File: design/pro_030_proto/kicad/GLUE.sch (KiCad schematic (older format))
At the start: 26 parts, among them IC3 ATF16V8BQL-15PU

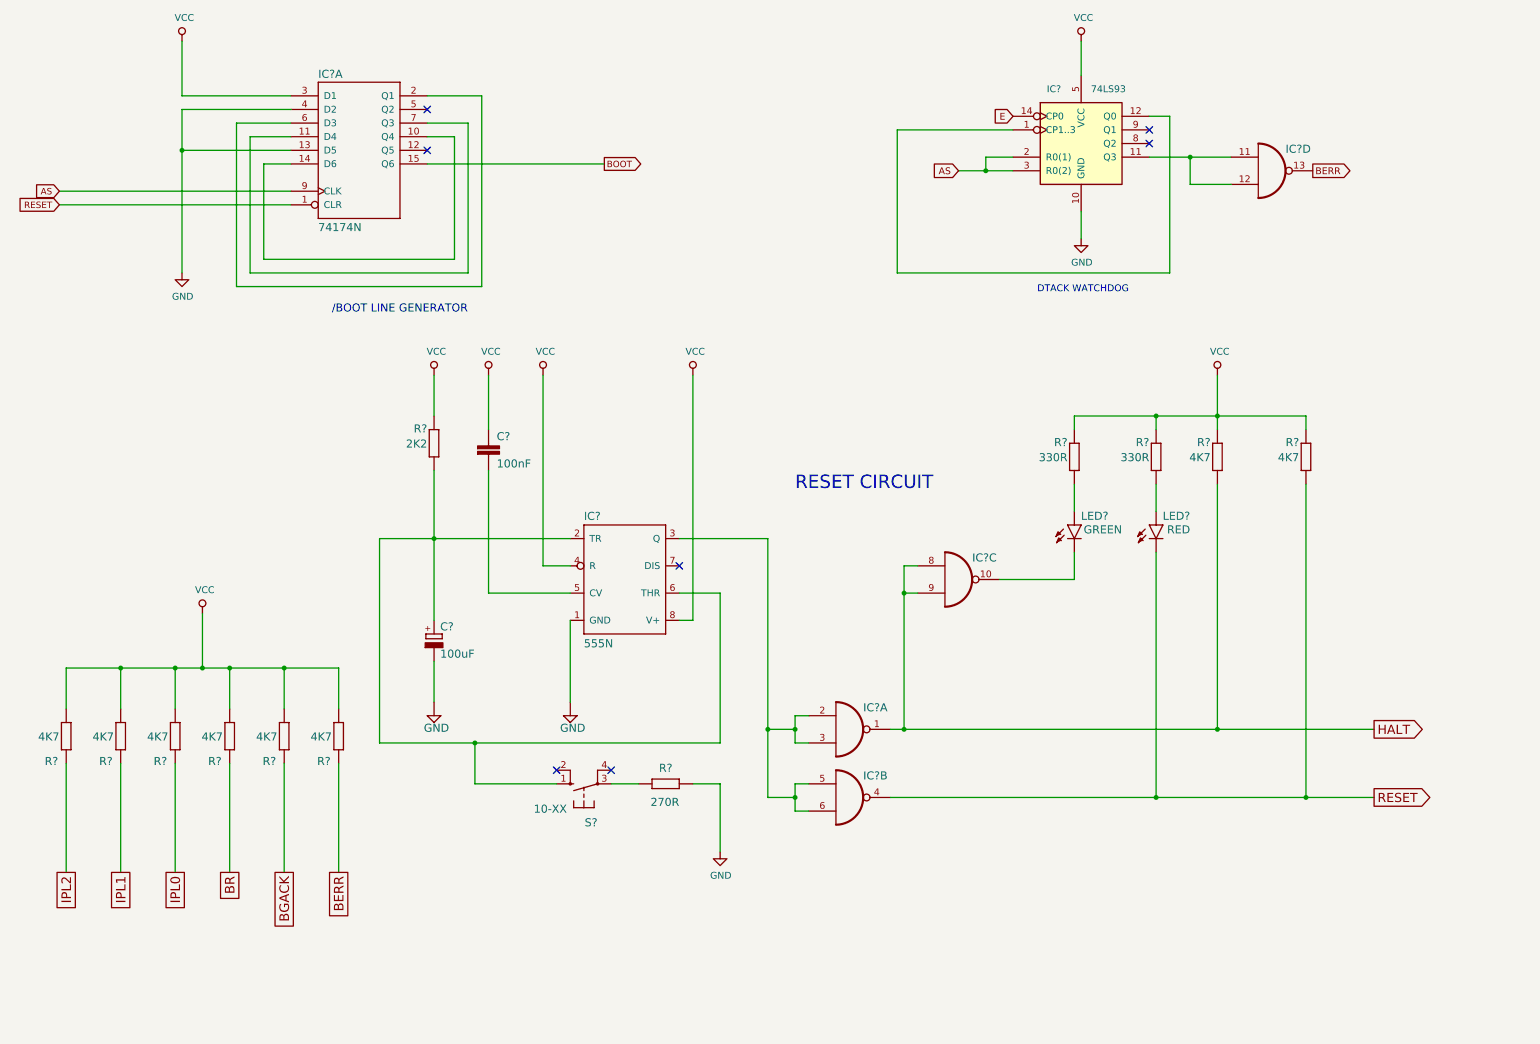
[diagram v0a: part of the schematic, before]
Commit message: Add interrupt glue to schematic
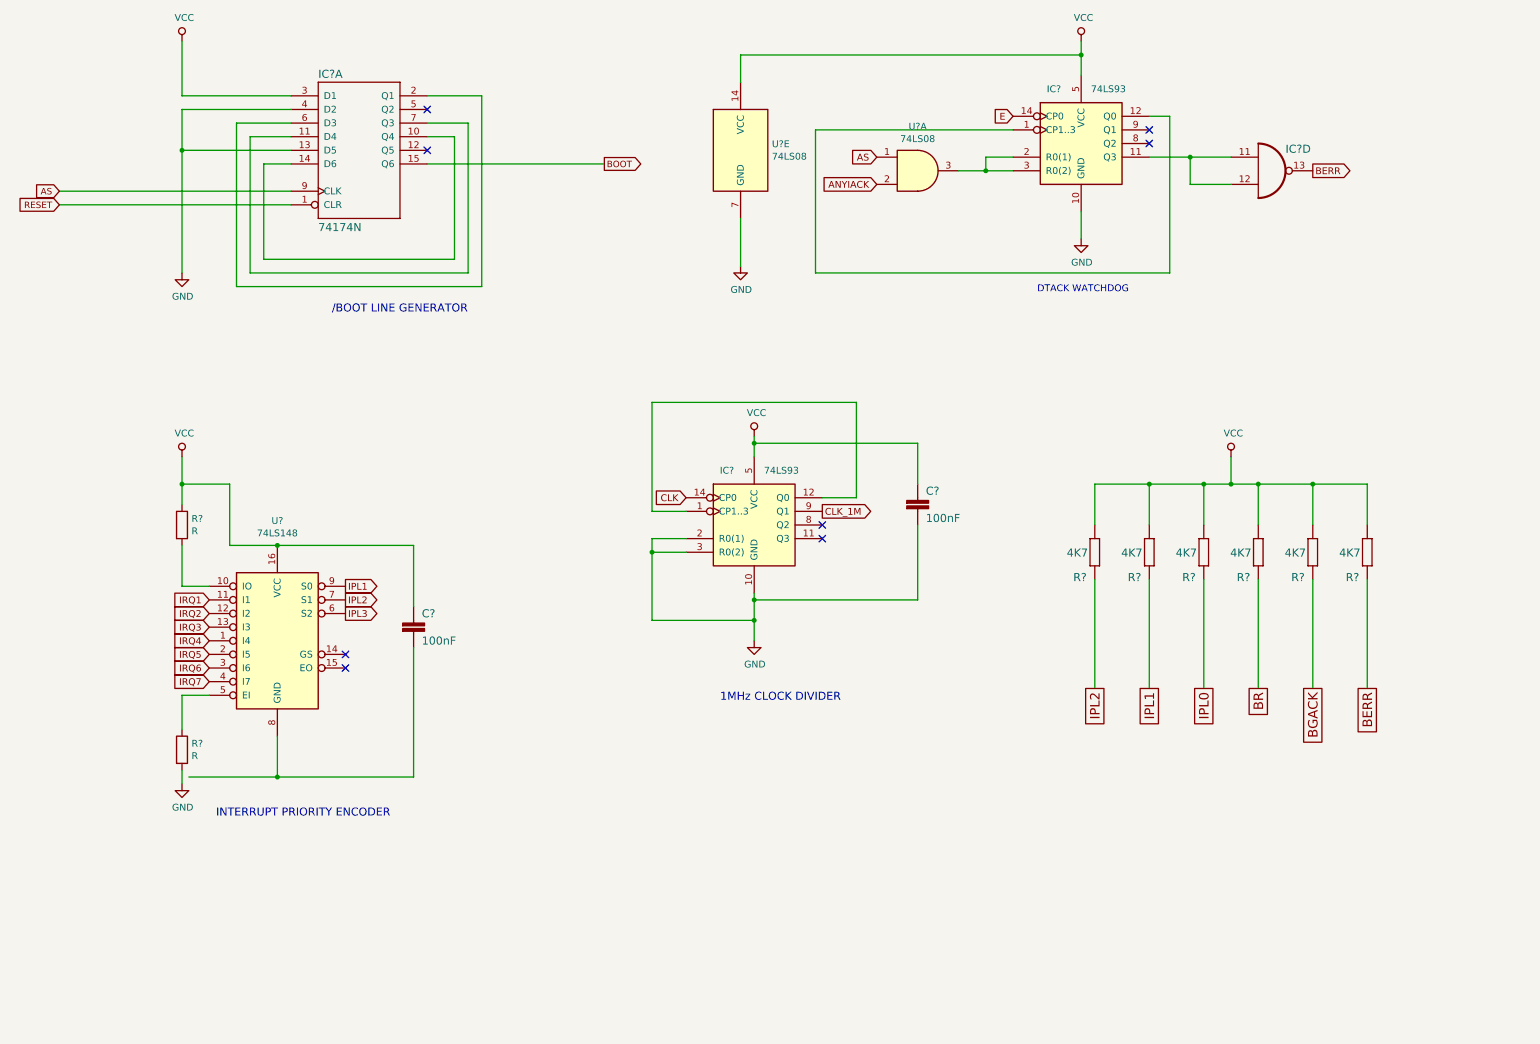
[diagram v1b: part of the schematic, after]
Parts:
- removed C?: 100nF, rosco_m68k:C2.5-3, symbol rosco_m68k-eagle-import:C2,5-3
- removed C?: 100uF, rosco_m68k:E2,5-5, symbol rosco_m68k-eagle-import:CPOL-EUE2.5-5
- removed IC?: 555N, Package_DIP:DIP-8_W7.62mm_LongPads, symbol rosco_m68k-eagle-import:555N
- removed IC? (x3): 74LS01N, Package_DIP:DIP-14_W7.62mm_Socket_LongPads, symbol rosco_m68k-eagle-import:7401N
- removed LED?: RED, rosco_m68k:LED5MM, symbol rosco_m68k-eagle-import:LED5MM
- removed LED?: GREEN, rosco_m68k:LED5MM, symbol rosco_m68k-eagle-import:LED5MM
- removed R?: 2K2, rosco_m68k:0207_10, symbol rosco_m68k-eagle-import:R-EU_0207_10
- removed R?: 270R, rosco_m68k:0207_10, symbol rosco_m68k-eagle-import:R-EU_0207_10
- removed R? (x2): 330R, rosco_m68k:0207_10, symbol rosco_m68k-eagle-import:R-EU_0207_10
- removed R? (x2): 4K7, rosco_m68k:0207_10, symbol rosco_m68k-eagle-import:R-EU_0207_10
- removed S?: 10-XX, rosco_m68k:B3F-10XX, symbol rosco_m68k-eagle-import:10-XX
- added C? (x2): 100nF, rosco_m68k:C2.5-3, symbol rosco_m68k-eagle-import:C2,5-3
- added IC?: 74LS93, Package_DIP:DIP-14_W7.62mm_Socket_LongPads, symbol 74xx:74LS93
- added R? (x2): R, symbol Device:R
- added U? (x2): 74LS08, symbol 74xx:74LS08
- added U?: 74LS148, symbol 74xx:74LS148
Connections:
- net labels added: ANYIACK, CLK, CLK_1M, IPL3, IRQ1, IRQ2, IRQ3, IRQ4, IRQ5, IRQ6, IRQ7
- net labels removed: HALT
- wire segments 139 -> 116
- no-connect marks 9 -> 10
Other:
- note added: "1MHz CLOCK DIVIDER"
- note added: "INTERRUPT PRIORITY ENCODER"
- note removed: "RESET CIRCUIT"
- moved on the sheet: R?

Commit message: Largeish changeset:
* Added (first-cut) glue for DTACK generation
* Fix mem selects to use new DTACK generation
* Add missing footprints for Kicad
* Add POWER and TESTPOINTS schematics
* Update footprints across the board to allow error-free PCB import
* Pull all components (so far) into PCB
* Fix MC68030RC footprint (missing pads)
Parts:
- removed C13: 100nF, rosco_m68k:C2.5-3, symbol rosco_m68k-eagle-import:C2,5-3
- removed IC3: ATF16V8BQL-15PU, rosco_m68k:DIL20, symbol rosco_m68k-eagle-import:ATF16V8BP3
- removed R? (x6): 4K7, rosco_m68k:0207_10, symbol rosco_m68k-eagle-import:R-EU_0207_10
- removed U?: 74LS08, symbol 74xx:74LS08
- added X2: 8MHz, Oscillator:Oscillator_DIP-8, symbol Oscillator:CXO_DIP8
- IC12: renamed from U?; footprint (none) -> Package_DIP:DIP-16_W7.62mm_Socket_LongPads
- IC13: renamed from U?; footprint (none) -> Package_DIP:DIP-14_W7.62mm_LongPads
- R24, R25: renamed from R?; footprint (none) -> rosco_m68k:R-0207_10
- gave numbers to parts that had none: 6
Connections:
- net labels added: CLK_8M
- net labels removed: A10, A11, A12, A13, A14, A15, A16, A17, A18, A6, A7, A8, A9, A[1..23], BGACK, BR, CLK, IOSEL, IPL0, LDS, MFPSEL
- wire segments 116 -> 83
- no-connect marks 10 -> 8
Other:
- note added: "8MHz/1MHz PERIPHERAL CLOCK"
- note removed: "1MHz CLOCK DIVIDER"
- note removed: "MFPSEL.PLD"
- moved on the sheet: C5

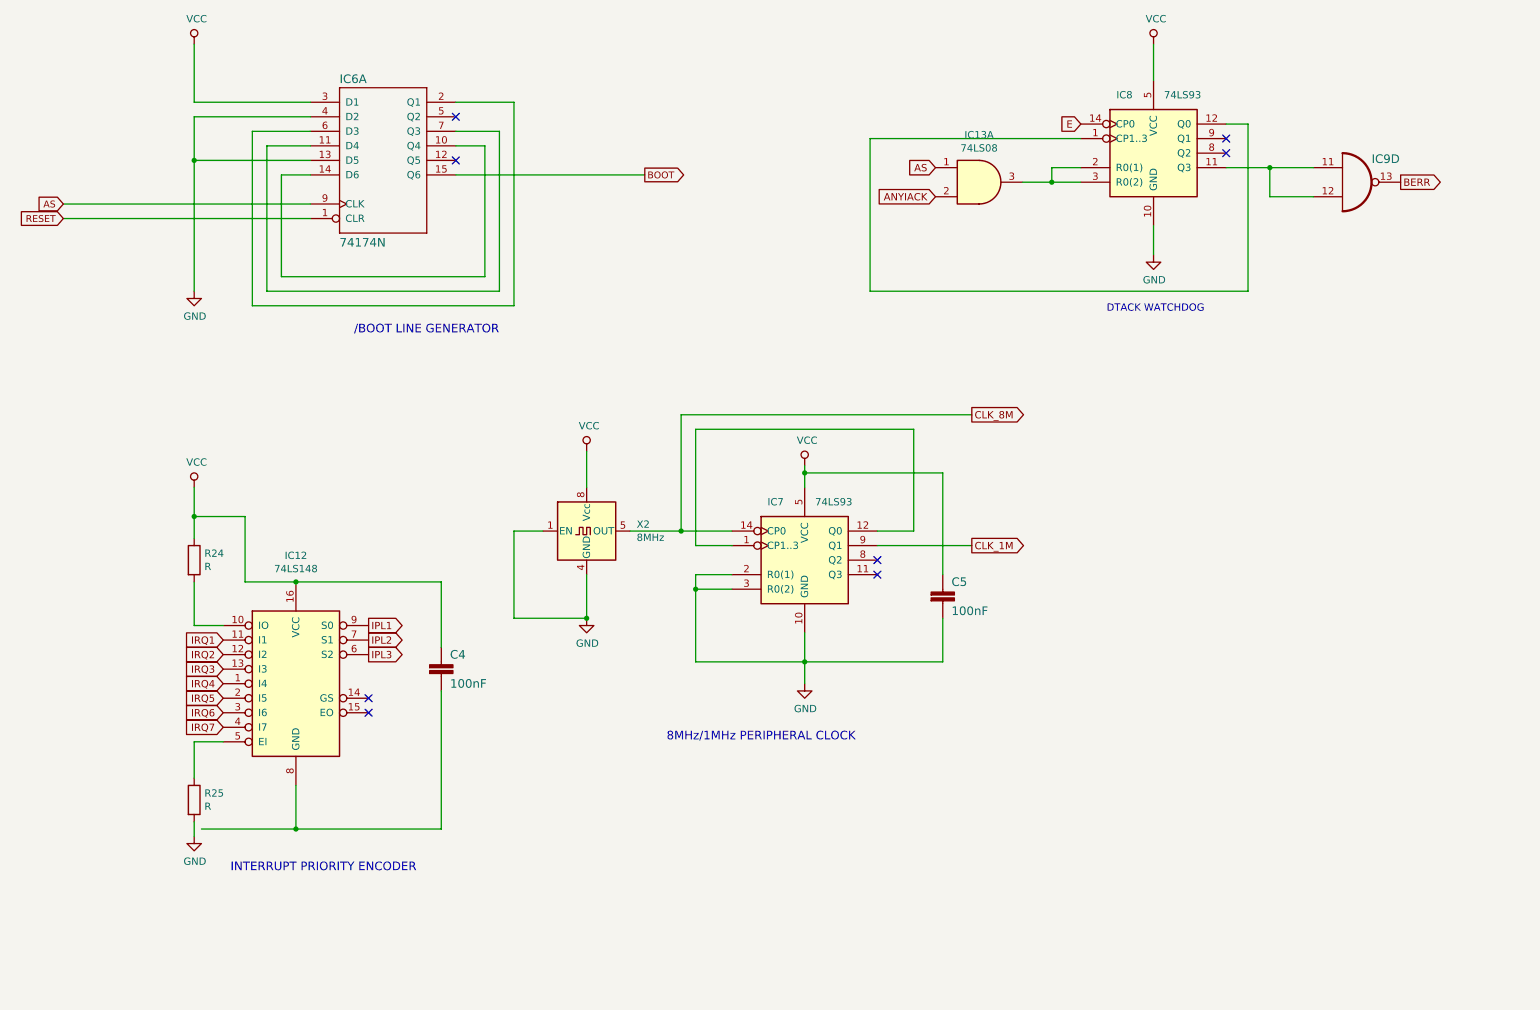
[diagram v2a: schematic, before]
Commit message: Add DTACK delays and fixes
* Add configurable DTACK delay for RAM & ROM
* Add DTACK generation for RAM/ROM with delay support in IC5
* Fix /BOOT line generator for 32-bit port
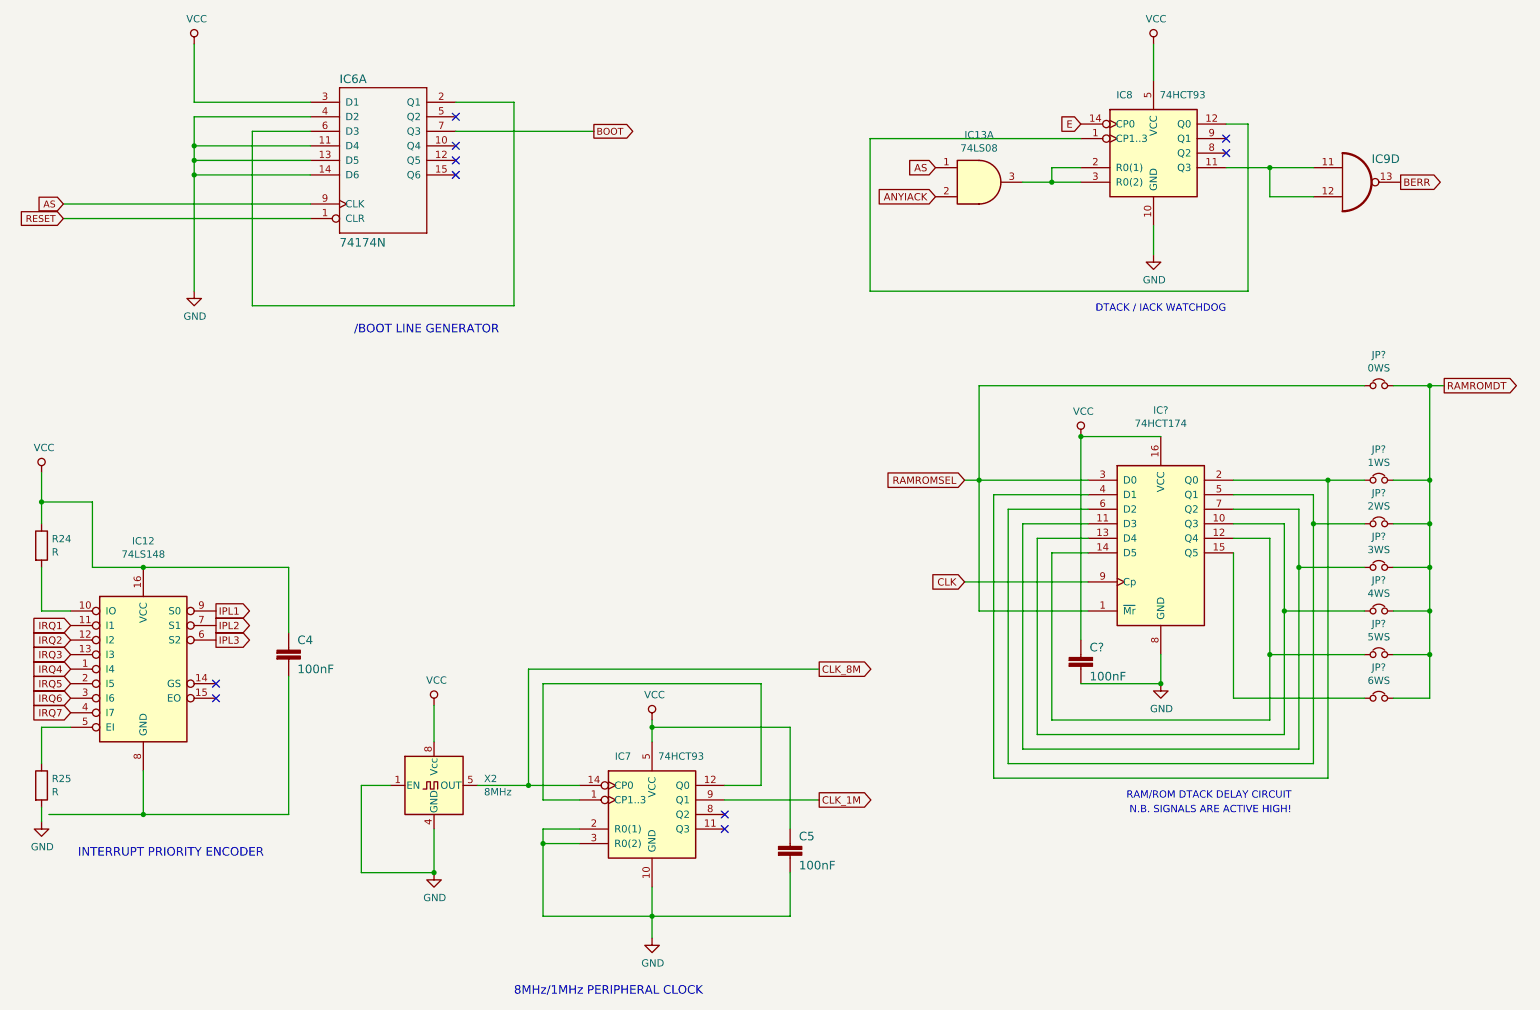
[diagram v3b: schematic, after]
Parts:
- added C?: 100nF, rosco_m68k:C2.5-3, symbol rosco_m68k-eagle-import:C2,5-3
- added IC?: 74HCT174, Package_DIP:DIP-16_W7.62mm_Socket_LongPads, symbol 74xx:74LS174
- added JP?: 0WS, rosco_m68k:pin-1X02, symbol Device:Jumper_NC_Small
- added JP?: 1WS, rosco_m68k:pin-1X02, symbol Device:Jumper_NC_Small
- added JP?: 2WS, rosco_m68k:pin-1X02, symbol Device:Jumper_NC_Small
- added JP?: 3WS, rosco_m68k:pin-1X02, symbol Device:Jumper_NC_Small
- added JP?: 4WS, rosco_m68k:pin-1X02, symbol Device:Jumper_NC_Small
- added JP?: 5WS, rosco_m68k:pin-1X02, symbol Device:Jumper_NC_Small
- added JP?: 6WS, rosco_m68k:pin-1X02, symbol Device:Jumper_NC_Small
- IC7, IC8: value 74LS93 -> 74HCT93
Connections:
- net BOOT: now also IC6.7 (Q3); no longer IC6.15 (Q6)
- net GND: now also IC6.11 (D4), IC6.14 (D6), C?.2, IC?.8 (GND)
- net VCC: now also C?.1, IC?.16 (VCC)
- net at IC6.10 (Q4): no longer IC6.14 (D6)
- new net: IC?.10 (Q3), IC?.13 (D4), JP?.1
- new net: IC?.11 (D3), IC?.7 (Q2), JP?.1
- new net: IC?.12 (Q4), IC?.14 (D5), JP?.1
- new net: IC?.15 (Q5), JP?.1
- new net: IC?.2 (Q0), IC?.4 (D1), JP?.1
- new net: IC?.5 (Q1), IC?.6 (D2), JP?.1
- new net CLK: IC?.9 (Cp)
- new net RAMROMDT: JP?.2, JP?.2, JP?.2, JP?.2, JP?.2, JP?.2, JP?.2
- new net RAMROMSEL: IC?.1 (~Mr), IC?.3 (D0), JP?.1
- no-connect marks 8 -> 10
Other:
- note added: "DTACK / IACK WATCHDOG"
- note added: "N.B. SIGNALS ARE ACTIVE HIGH!"
- note added: "RAM/ROM DTACK DELAY CIRCUIT"
- note removed: "DTACK WATCHDOG"
- moved on the sheet: C4, C5, IC12, IC7, R24, R25, X2

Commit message: Make DTACK delay input selectable, and update netlist
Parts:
- added JP12: FAST, rosco_m68k:pin-1X02, symbol Device:Jumper_NC_Small
- added JP13: SLOW, rosco_m68k:pin-1X02, symbol Device:Jumper_NC_Small
- added JP14: SLOWEST, rosco_m68k:pin-1X02, symbol Device:Jumper_NC_Small
- gave numbers to parts that had none: 9
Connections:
- net CLK: now also JP12.1; no longer IC14.9 (Cp)
- net CLK_1M: now also IC7.8 (Q2), JP14.1; no longer IC7.9 (Q1)
- net CLK_8M: now also JP13.1
- new net: IC14.9 (Cp), JP12.2, JP13.2, JP14.2
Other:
- note added: "8MHz/1MHz AUXILLIARY CLOCKS"
- note added: "N.B. RAMROMSEL AND RAMROMDT ARE ACTIVE HIGH!"
- note removed: "8MHz/1MHz PERIPHERAL CLOCK"
- note removed: "N.B. SIGNALS ARE ACTIVE HIGH!"
- moved on the sheet: C4, C5, IC12, IC7, R24, R25, X2

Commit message: Interrupts + Xosera schematic, re-annotate
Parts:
- renumbered C4 to C12, C5 to C13, C13 to C14, IC12 to IC3, IC6 to IC4, IC7 to IC5, IC13 to IC6, IC8 to IC7, IC14 to IC8, JP7 to JP10, JP8 to JP11, JP9 to JP12, JP10 to JP13, JP11 to JP14, JP12 to JP5, JP13 to JP6, JP14 to JP7, JP5 to JP8, JP6 to JP9
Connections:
- net GND: now also C12.2, IC3.8 (GND)
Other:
- moved on the sheet: C12, IC3, R24, R25

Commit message: Big(ish) push on placement
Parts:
- removed C12: 100nF, rosco_m68k:C2.5-3, symbol rosco_m68k-eagle-import:C2,5-3
- removed IC3: 74LS148, Package_DIP:DIP-16_W7.62mm_Socket_LongPads, symbol 74xx:74LS148
- removed R24, R25: R, rosco_m68k:R-0207_10, symbol Device:R
- added unit 2 of IC6
- added unit 3 of IC6
- added unit 4 of IC6
- C13, C14: footprint rosco_m68k:C2.5-3 -> Capacitor_THT:C_Rect_L4.0mm_W2.5mm_P2.50mm
- JP10, JP11, JP12, JP13, JP14, JP5, JP6, JP7, JP8, JP9: footprint rosco_m68k:pin-1X02 -> Connector_PinHeader_2.54mm:PinHeader_1x02_P2.54mm_Vertical
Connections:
- net E is gone; now on net CLK_1M: IC7.14 (CP0)
- net GND: now also IC6.10, IC6.12, IC6.13, IC6.4, IC6.5, IC6.9
- no-connect marks 10 -> 11
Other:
- note removed: "INTERRUPT PRIORITY ENCODER"
- moved on the sheet: C13, IC5, X2
